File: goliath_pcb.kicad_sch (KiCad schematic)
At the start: 101 parts, among them J1 RJ45_LED, J10 Conn_01x04_Male, J11 Screw_Terminal_01x02, J12 Screw_Terminal_01x02, J13 Screw_Terminal_01x02, J14 Conn_01x02_Male, J15 Conn_01x02_Male, J2 RJ45_LED, J3 RJ45_LED, J4 RJ45_LED, J5 Conn_01x08_Male, J6 Conn_01x08_Male, J7 Conn_01x02_Male, J8 Conn_01x04_Male, J9 Conn_01x04_Male, Q1 STP2N80K5, Q2 STP2N80K5, SW1 SW_Push, U1 Pico, U2 LM2592HVT-5.0/NOPB, U3 74HCT244, U4 74HCT244, U5 MCP3008, U6 PCF8574, U7 PCF8574

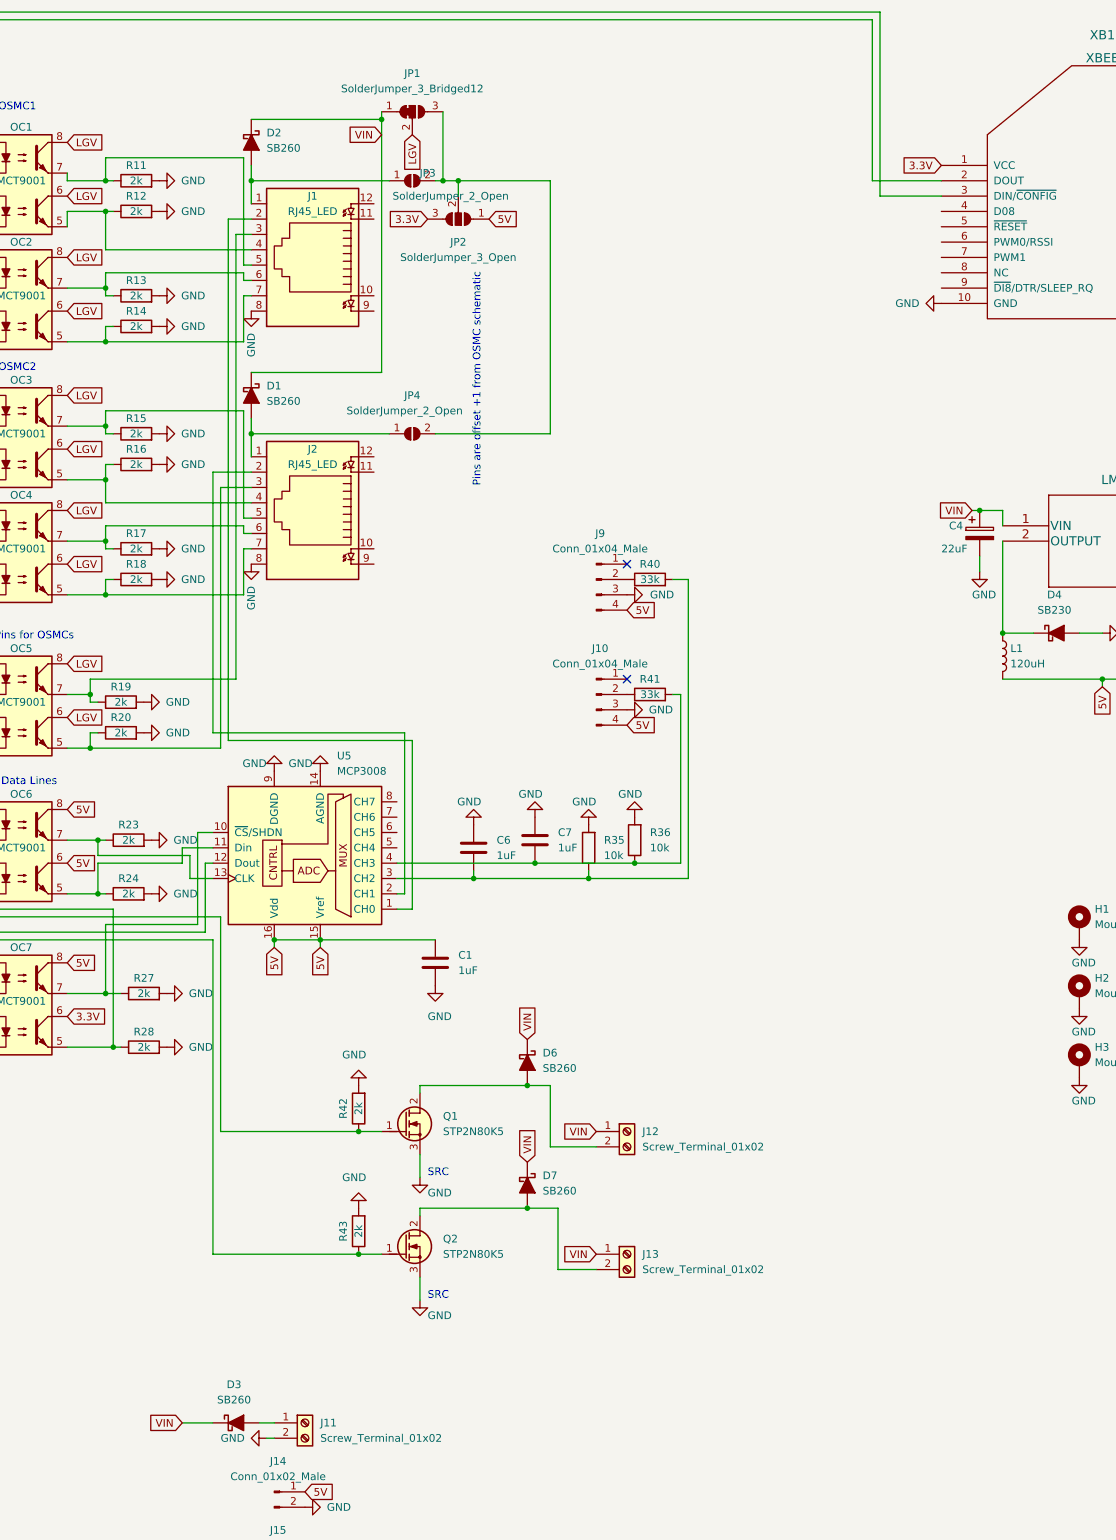
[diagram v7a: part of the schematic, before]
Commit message: Add power switch, add more text, cleanup
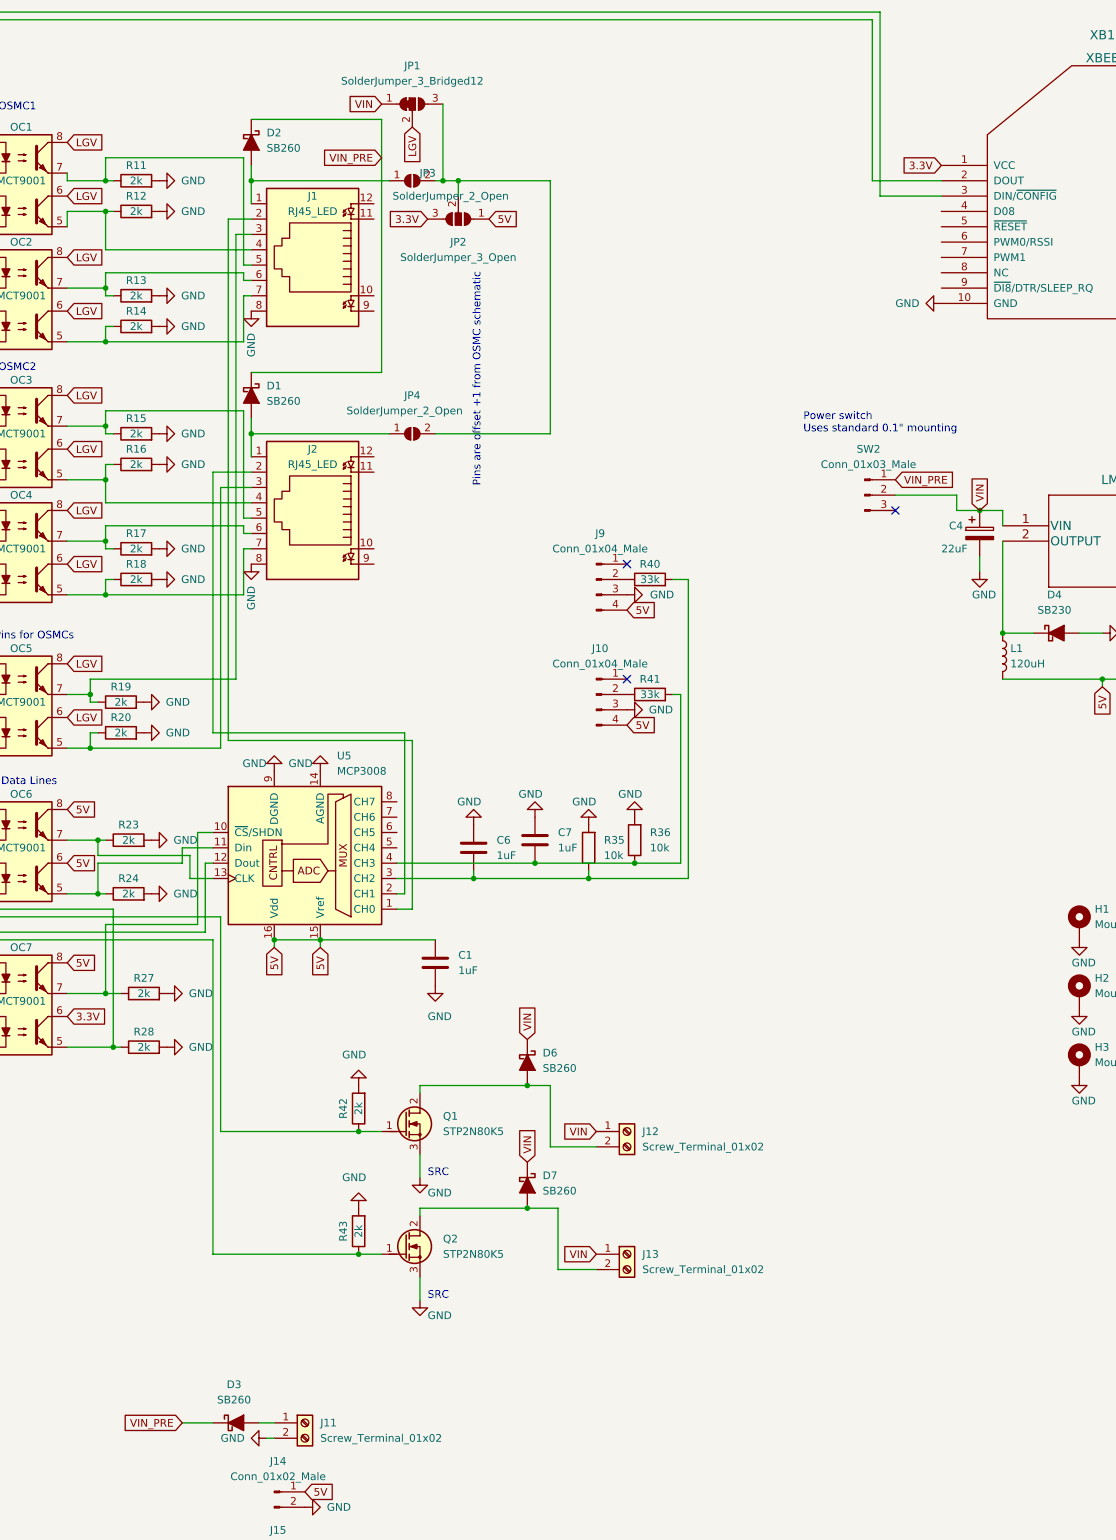
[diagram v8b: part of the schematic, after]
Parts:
- added SW2: Conn_01x03_Male, Connector_PinSocket_2.54mm:PinSocket_1x03_P2.54mm_Vertical, symbol Connector:Conn_01x03_Male
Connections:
- net VIN: now also SW2.2 (Pin_2); no longer D1.1 (K), D2.1 (K), D3.1 (K)
- new net VIN_PRE: D1.1 (K), D2.1 (K), D3.1 (K), SW2.1 (Pin_1)
- no-connect marks 2 -> 3
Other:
- note added: "Power switch Uses standard 0.1" mounting"
- moved on the sheet: JP1
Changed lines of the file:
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@@
   (junction (at 129.54 234.95) (diameter 0) (color 0 0 0 0)
   )
-  (junction (at 233.68 36.83) (diameter 0) (color 0 0 0 0)
-  )
   (junction (at 116.84 238.76) (diameter 0) (color 0 0 0 0)
   )
@@
   (no_connect (at 274.32 129.54))
   (no_connect (at 274.32 110.49))
+  (no_connect (at 318.77 101.6))
   (wire (pts (xy 210.82 85.09) (xy 210.82 102.87))
     (stroke (width 0) (type default) (color 0 0 0 0))
@@
     (stroke (width 0) (type default) (color 0 0 0 0))
   )
-  (wire (pts (xy 331.47 101.6) (xy 332.74 101.6))
+  (wire (pts (xy 328.93 101.6) (xy 332.74 101.6))
     (stroke (width 0) (type default) (color 0 0 0 0))
   )
@@
     (stroke (width 0) (type default) (color 0 0 0 0))
   )
-  (wire (pts (xy 233.68 35.56) (xy 233.68 36.83))
-    (stroke (width 0) (type default) (color 0 0 0 0))
-  )
   (wire (pts (xy 205.74 95.25) (xy 212.09 95.25))
     (stroke (width 0) (type default) (color 0 0 0 0))
@@
     (stroke (width 0) (type default) (color 0 0 0 0))
   )
+  (wire (pts (xy 328.93 101.6) (xy 328.93 99.06))
+    (stroke (width 0) (type default) (color 0 0 0 0))
+  )
   (wire (pts (xy 71.12 222.25) (xy 81.28 222.25))
     (stroke (width 0) (type default) (color 0 0 0 0))
@@
     (stroke (width 0) (type default) (color 0 0 0 0))
   )
-  (wire (pts (xy 243.84 35.56) (xy 243.84 46.99))
+  (wire (pts (xy 243.84 34.29) (xy 243.84 46.99))
     (stroke (width 0) (type default) (color 0 0 0 0))
   )
@@
     (stroke (width 0) (type default) (color 0 0 0 0))
   )
+  (wire (pts (xy 328.93 99.06) (xy 318.77 99.06))
+    (stroke (width 0) (type default) (color 0 0 0 0))
+  )
   (wire (pts (xy 81.28 190.5) (xy 81.28 189.23))
     (stroke (width 0) (type default) (color 0 0 0 0))
@@
     (effects (font (size 1.27 1.27)) (justify left bottom))
   )
+  (text "Power switch\nUses standard 0.1\" mounting" (at 303.53 88.9 0)
+    (effects (font (size 1.27 1.27)) (justify left bottom))
+  )
   (text "Orange" (at 123.19 243.84 0)
     (effects (font (size 1.27 1.27)) (justify left bottom))
@@
     )
   )
-  (global_label "5V" (shape input) (at 223.52 173.99 270) (fields_autoplaced)
+  (global_label "VIN_PRE" (shape input) (at 200.66 252.73 180) (fields_autoplaced)
     (effects (font (size 1.27 1.27)) (justify right))
-    (property "Intersheet References" "${INTERSHEET_REFS}" (id 0) (at 223.5994 178.7012 90)
+    (property "Intersheet References" "${INTERSHEET_REFS}" (id 0) (at 190.5664 252.8094 0)
       (effects (font (size 1.27 1.27)) (justify right) hide)
     )
   )
-  (global_label "VIN" (shape input) (at 331.47 101.6 180) (fields_autoplaced)
+  (global_label "5V" (shape input) (at 223.52 173.99 270) (fields_autoplaced)
     (effects (font (size 1.27 1.27)) (justify right))
-    (property "Intersheet References" "${INTERSHEET_REFS}" (id 0) (at 326.0331 101.5206 0)
+    (property "Intersheet References" "${INTERSHEET_REFS}" (id 0) (at 223.5994 178.7012 90)
       (effects (font (size 1.27 1.27)) (justify right) hide)
     )
   )
-  (global_label "VIN" (shape input) (at 233.68 39.37 180) (fields_autoplaced)
+  (global_label "VIN_PRE" (shape input) (at 233.68 43.18 180) (fields_autoplaced)
     (effects (font (size 1.27 1.27)) (justify right))
-    (property "Intersheet References" "${INTERSHEET_REFS}" (id 0) (at 228.2431 39.2906 0)
+    (property "Intersheet References" "${INTERSHEET_REFS}" (id 0) (at 223.5864 43.2594 0)
       (effects (font (size 1.27 1.27)) (justify right) hide)
     )
@@
     )
   )
-  (global_label "LGV" (shape input) (at 238.76 39.37 270) (fields_autoplaced)
+  (global_label "LGV" (shape input) (at 238.76 38.1 270) (fields_autoplaced)
     (effects (font (size 1.27 1.27)) (justify right))
-    (property "Intersheet References" "${INTERSHEET_REFS}" (id 0) (at 238.6806 45.1698 90)
+    (property "Intersheet References" "${INTERSHEET_REFS}" (id 0) (at 238.6806 43.8998 90)
       (effects (font (size 1.27 1.27)) (justify right) hide)
     )
@@
     )
   )
+  (global_label "VIN" (shape input) (at 332.74 101.6 90) (fields_autoplaced)
+    (effects (font (size 1.27 1.27)) (justify left))
+    (property "Intersheet References" "${INTERSHEET_REFS}" (id 0) (at 332.8194 96.1631 90)
+      (effects (font (size 1.27 1.27)) (justify left) hide)
+    )
+  )
   (global_label "5V" (shape input) (at 220.98 275.59 0) (fields_autoplaced)
     (effects (font (size 1.27 1.27)) (justify left))
@@
     )
   )
+  (global_label "VIN" (shape input) (at 233.68 34.29 180) (fields_autoplaced)
+    (effects (font (size 1.27 1.27)) (justify right))
+    (property "Intersheet References" "${INTERSHEET_REFS}" (id 0) (at 228.2431 34.2106 0)
+      (effects (font (size 1.27 1.27)) (justify right) hide)
+    )
+  )
   (global_label "5V" (shape input) (at 181.61 160.02 0) (fields_autoplaced)
     (effects (font (size 1.27 1.27)) (justify left))
@@
     )
   )
-  (global_label "VIN" (shape input) (at 200.66 252.73 180) (fields_autoplaced)
-    (effects (font (size 1.27 1.27)) (justify right))
-    (property "Intersheet References" "${INTERSHEET_REFS}" (id 0) (at 195.2231 252.6506 0)
-      (effects (font (size 1.27 1.27)) (justify right) hide)
-    )
-  )
   (global_label "VIN" (shape input) (at 269.24 224.79 180) (fields_autoplaced)
     (effects (font (size 1.27 1.27)) (justify right))
@@
     )
   )
+  (global_label "VIN_PRE" (shape input) (at 318.77 96.52 0) (fields_autoplaced)
+    (effects (font (size 1.27 1.27)) (justify left))
+    (property "Intersheet References" "${INTERSHEET_REFS}" (id 0) (at 328.8636 96.4406 0)
+      (effects (font (size 1.27 1.27)) (justify left) hide)
+    )
+  )
   (global_label "3.3V" (shape input) (at 326.39 44.45 180) (fields_autoplaced)
     (effects (font (size 1.27 1.27)) (justify right))
@@
     (pin "1")
   )
-  (symbol (lib_id "Jumper:SolderJumper_3_Bridged12") (at 238.76 35.56 0) (unit 1)
+  (symbol (lib_id "Jumper:SolderJumper_3_Bridged12") (at 238.76 34.29 0) (unit 1)
     (in_bom yes) (on_board yes) (fields_autoplaced)
-    (property "Reference" "JP1" (id 0) (at 238.76 29.21 0))
-    (property "Value" "SolderJumper_3_Bridged12" (id 1) (at 238.76 31.75 0))
-    (property "Footprint" "Jumper:SolderJumper-3_P1.3mm_Open_Pad1.0x1.5mm" (id 2) (at 238.76 35.56 0)
+    (property "Reference" "JP1" (id 0) (at 238.76 27.94 0))
+    (property "Value" "SolderJumper_3_Bridged12" (id 1) (at 238.76 30.48 0))
+    (property "Footprint" "Jumper:SolderJumper-3_P1.3mm_Open_Pad1.0x1.5mm" (id 2) (at 238.76 34.29 0)
       (effects (font (size 1.27 1.27)) hide)
     )
-    (property "Datasheet" "~" (id 3) (at 238.76 35.56 0)
+    (property "Datasheet" "~" (id 3) (at 238.76 34.29 0)
       (effects (font (size 1.27 1.27)) hide)
     )
@@
     (pin "2")
   )
+  (symbol (lib_id "Connector:Conn_01x03_Male") (at 313.69 99.06 0) (unit 1)
+    (in_bom yes) (on_board yes) (fields_autoplaced)
+    (property "Reference" "SW2" (id 0) (at 314.325 91.44 0))
+    (property "Value" "Conn_01x03_Male" (id 1) (at 314.325 93.98 0))
+    (property "Footprint" "Connector_PinSocket_2.54mm:PinSocket_1x03_P2.54mm_Vertical" (id 2) (at 313.69 99.06 0)
+      (effects (font (size 1.27 1.27)) hide)
+    )
+    (property "Datasheet" "~" (id 3) (at 313.69 99.06 0)
+      (effects (font (size 1.27 1.27)) hide)
+    )
+    (pin "1")
+    (pin "2")
+    (pin "3")
+  )
   (symbol (lib_id "Device:R") (at 162.56 160.02 90) (unit 1)
     (in_bom yes) (on_board yes)
@@
       (reference "SW1") (unit 1) (value "SW_Push") (footprint "4.5mm_button:SW_Tactile_PUSH_4.5mm_H3.8mm_TS_C016")
     )
+    (path "/a223c2a6-e8be-4db3-838f-bf9daa318711"
+      (reference "SW2") (unit 1) (value "Conn_01x03_Male") (footprint "Connector_PinSocket_2.54mm:PinSocket_1x03_P2.54mm_Vertical")
+    )
     (path "/cb20d2a1-05a5-401a-9981-368013b11a84"
